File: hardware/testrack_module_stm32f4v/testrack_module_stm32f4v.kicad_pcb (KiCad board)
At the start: 4 copper layers, 38 x 38 mm, 22 parts, among them J1 Bus_M.2_Socket_B, U1 STM32F407VGTx, U2 LT1962-3.3, U3 24AA01-I/SN, Y1 32.768kHz, Y2 12MHz

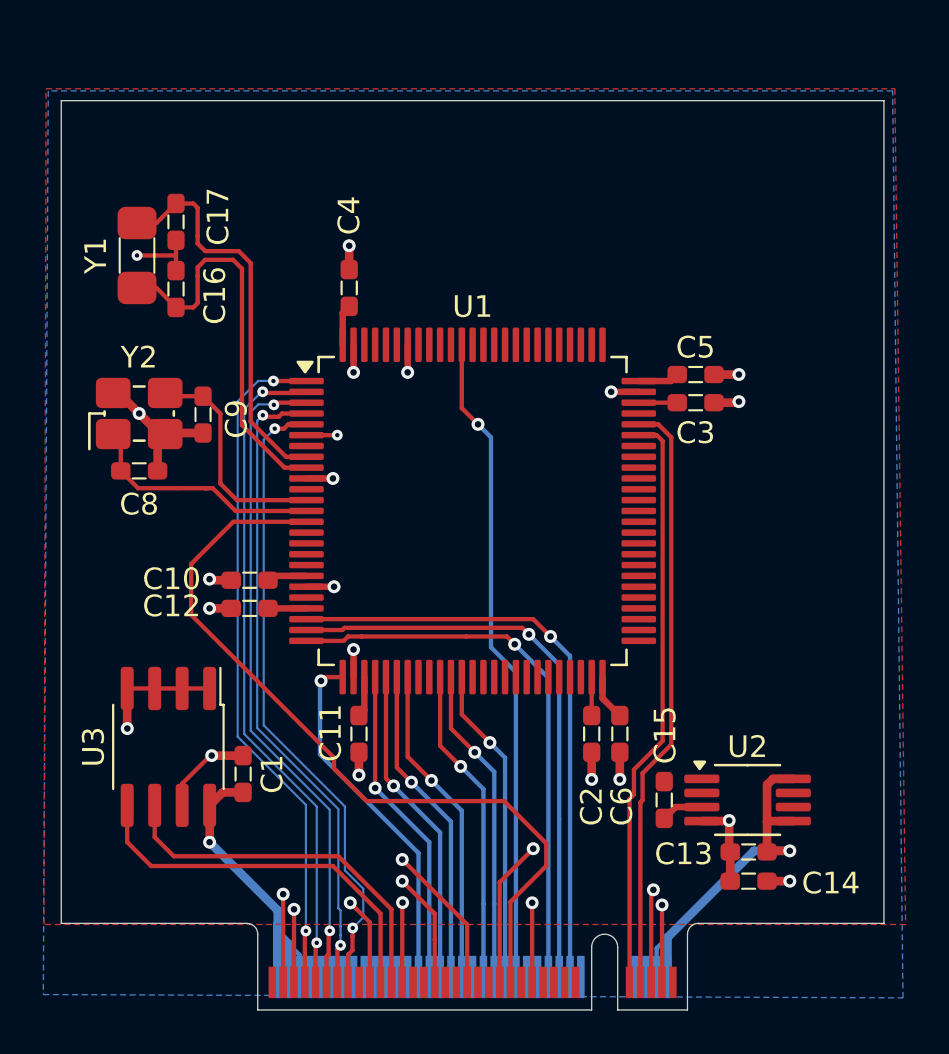
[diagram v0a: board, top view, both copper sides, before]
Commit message: Added the mounting hole to the target board
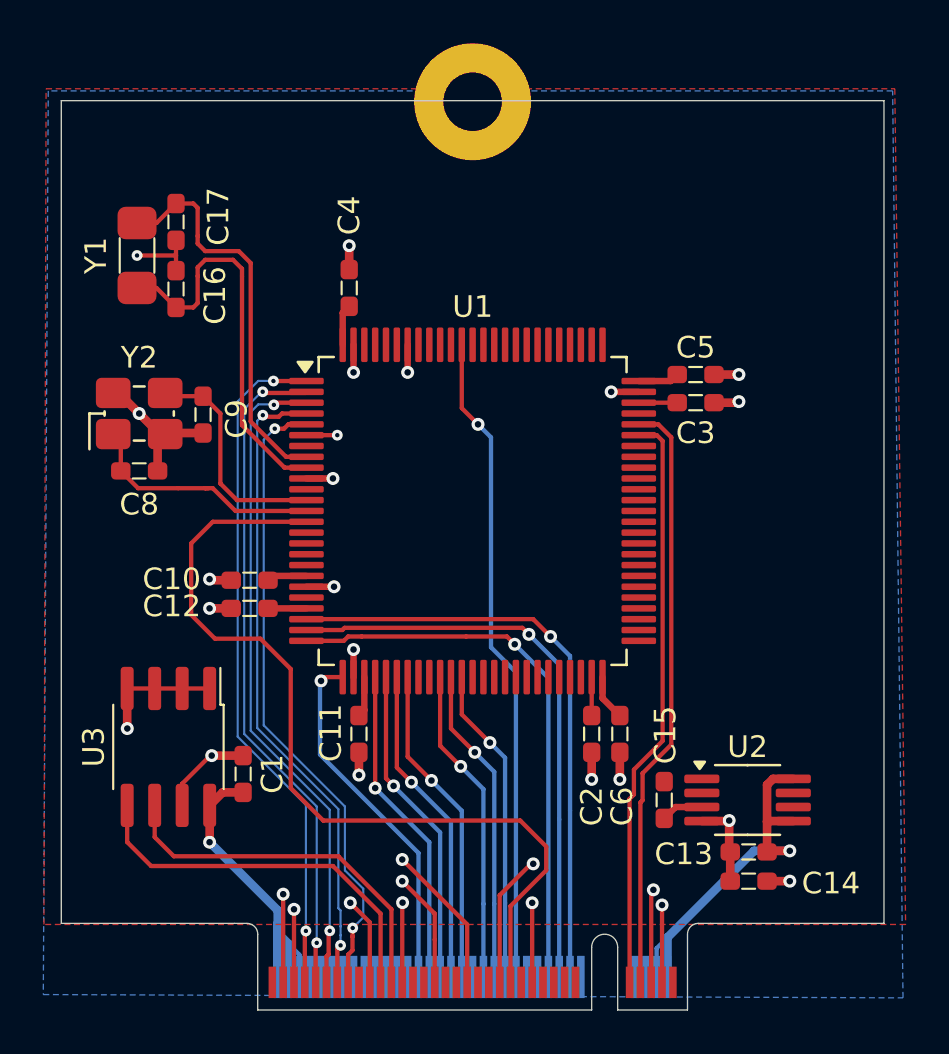
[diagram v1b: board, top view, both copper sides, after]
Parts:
- added H1: MountingHole_Pad, MountingHole:MountingHole_2.7mm_M2.5_Pad, F.Cu at (89.0, 69.4)
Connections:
- net /NRST renamed /~{RST}
- J1 pad 28: unconnected-(J1-GPIO_8-Pad28) -> +3.3V
- J1 pad 30: /JTMS -> /TMS
- J1 pad 32: /JTCK -> /TCK
- J1 pad 34: /JTDI -> /TDI
- J1 pad 36: /JTDO -> /TDO
- J1 pad 38: unconnected-(J1-DEVSLP-Pad38) -> +3.3V
- J1 pad 56: unconnected-(J1-NC-Pad56) -> (no net)
- J1 pad 58: unconnected-(J1-NC-Pad58) -> (no net)
- J1 pad 59: unconnected-(J1-ANTCTL0-Pad59) -> (no net)
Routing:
- net /~{RST}: track 36.7 -> 40.1 mm
- net GND: track 86.5 -> 85.8 mm

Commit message: Added board identification on the silkscreen
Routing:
- net +3.3V: track 13.9 -> 54.4 mm, vias 2 -> 6
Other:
- board text added: "1"
- board text added: "1BitSquared"
- board text added: "2"
- board text added: "3"
- board text added: "4"
- board text added: "CERN OHL v2 Strict"
- board text added: "License"
- board text added: "RWK"
- board text added: "STM32F4V"
- board text added: "v0.1a"
